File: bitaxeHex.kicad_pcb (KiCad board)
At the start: 4 copper layers, 84.5 x 129.5 mm, 384 parts, among them J1 Screw Terminal, J2 Conn_01x01, J3 TC2030-IDC, J4 USB_C_Receptacle_USB2.0, J5 Conn_01x04, J6 Conn_01x04, J7 Conn_01x04, J8 ST7789 176x320, Q1 NTMFS5C673NLT1G, Q2 CSD17577Q5A, Q3 NTMFS5C673NLT1G, Q4 CSD17577Q5A, Q5 BSS123, Q6 2N7002K, SW1 EVQ-9P701P, SW2 EVQ-9P701P, U1 uA7805, U10 TMP1075, U11 TMP1075, U12 EMC2302, U13 BM1366_mode1, U14 ADP171AUJ-R7, U15 ADP171AUJ-R7, U16 BM1366_mode1, U17 25MHz, U18 TLV3544, U19 BM1366_mode0, U2 RT9080-33GJ5, U20 ADP171AUJ-R7, U21 ADP171AUJ-R7, U22 BM1366_mode0, U23 TLV3544, U24 BM1366_mode1, U25 ADP171AUJ-R7, U26 ADP171AUJ-R7, U27 BM1366_mode1, U28 25MHz, U3 INA219AIDCNR, U4 TPS40305, U5 MIC5504, U6 DS4432U+, U7 SN74AVC4T774, U8 25MHz, U9 ESP32-S3-WROOM-1, Y1 32.768kHz

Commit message: Fix some part numbers in the BOM
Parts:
- U3: value INA219AIDCNR -> INA219AID
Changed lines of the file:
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@@
     (descr "SOIC, 8 Pin (JEDEC MS-012AA, https://www.analog.com/media/en/package-pcb-resources/package/pkg_pdf/soic_narrow-r/r_8.pdf), generated with kicad-footprint-generator ipc_gullwing_generator.py")
     (tags "SOIC SO")
-    (property "DK" "296-23770-1-ND")
-    (property "PARTNO" "INA219AIDCNR")
+    (property "DK" "296-33291-5-ND")
+    (property "PARTNO" "INA219AID")
     (property "Sheetfile" "power.kicad_sch")
     (property "Sheetname" "Power")
@@
         (effects (font (size 1 1) (thickness 0.15)))
     )
-    (fp_text value "INA219AIDCNR" (at 0 3.4 -90) (layer "F.Fab")
+    (fp_text value "INA219AID" (at 0 3.4 -90) (layer "F.Fab")
         (effects (font (size 1 1) (thickness 0.15)))
     )

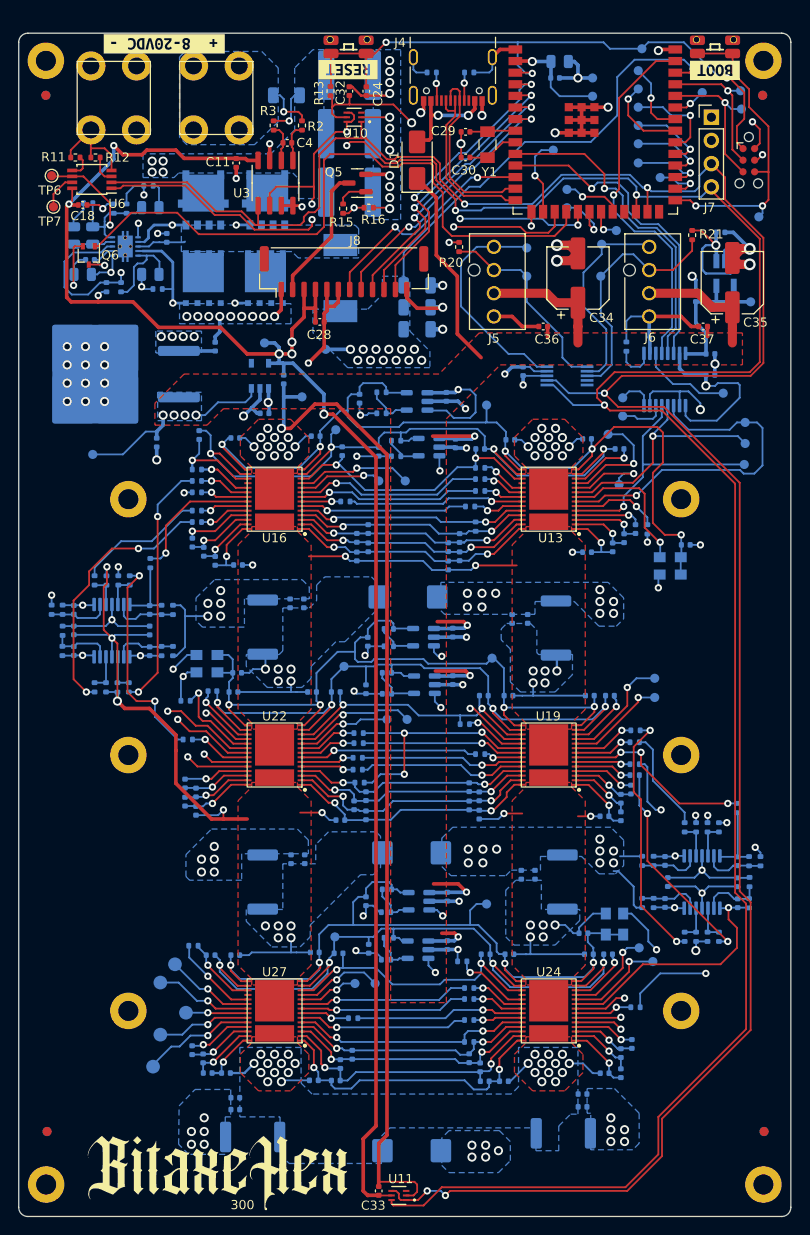
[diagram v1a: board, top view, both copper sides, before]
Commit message: mounting holes and fiducials
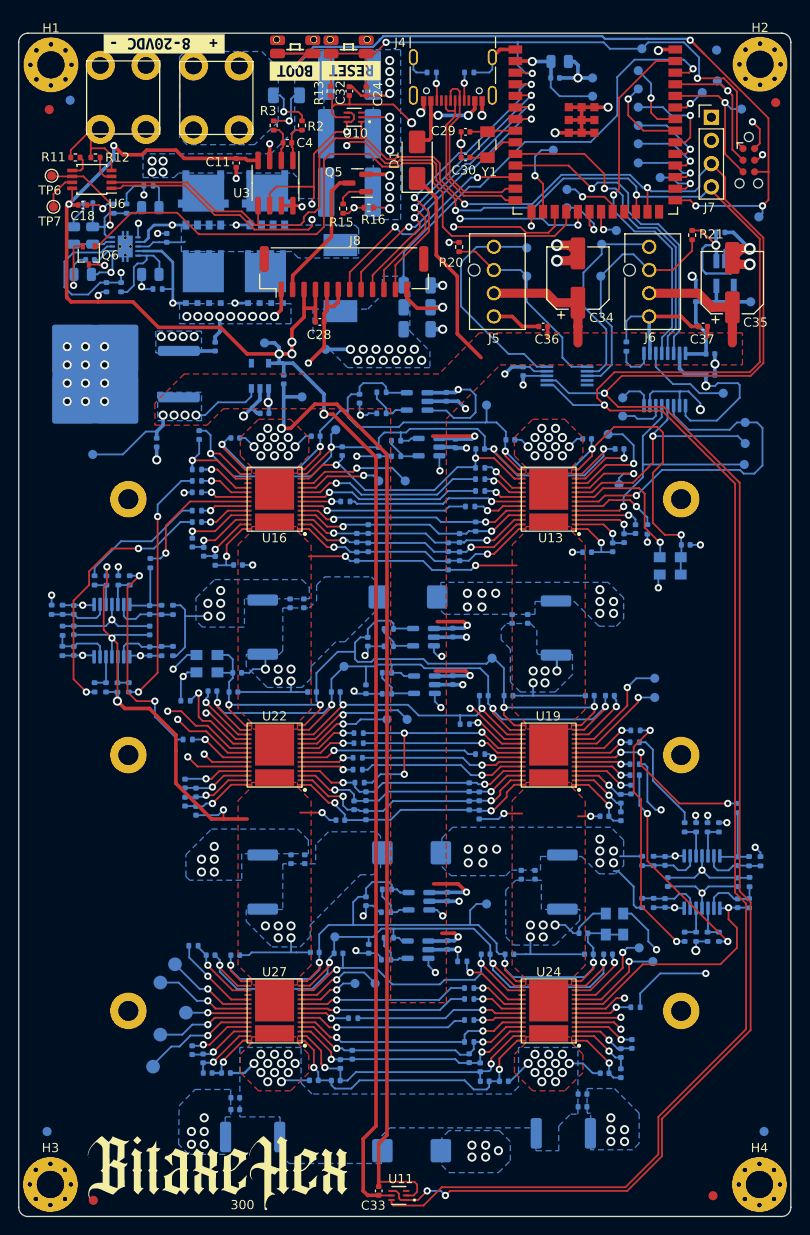
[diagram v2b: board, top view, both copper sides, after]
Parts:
- H1, H2, H3, H4: footprint bitaxe:4mm_mounting -> MountingHole:MountingHole_3mm_Pad_Via
- R25, R55, R87: value 130k 1% -> 69.8k 1%
- moved kibuzzard-65356D5C 46.0 mm to (80.2, 50.1)
- moved SW2 46.0 mm to (80.2, 47.5)
- moved FID7 9.08 mm to (58.2, 173.7)
- moved FID5 8.98 mm to (126.0, 173.2)
- moved FID8 7.06 mm to (126.4, 47.9)
- moved TP14 2.77 mm to (126.5, 51.2)
- moved FID6 2.71 mm to (55.6, 53.3)
- moved FID1 1.64 mm to (132.8, 53.6)
- moved FID3 1.60 mm to (53.3, 54.4)
- moved J2 1.03 mm to (61.4, 53.0)
- moved H1 0.70 mm to (53.5, 49.5)
- moved H2 0.57 mm to (131.1, 49.4)
- moved H3 0.47 mm to (53.5, 172.0)
- moved H4 0.44 mm to (131.1, 172.0)
- moved kibuzzard-65356D4E 0.34 mm to (86.4, 50.1)
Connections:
- net /BM1366-1/1V2 renamed /BM1366-1/1V8
- net /BM1366-2/1V2 renamed /BM1366-2/1V8
- net /BM1366-3/1V2 renamed /BM1366-3/1V8
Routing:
- net /ESP32/IO0: track 35.1 -> 85.8 mm, vias 2 -> 4
- net GND: track 427.1 -> 427.7 mm
- net /ESP32/EN: track 69.0 -> 69.5 mm

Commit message: fix mounting holes size/spacing, add pullup to PWR_EN signal
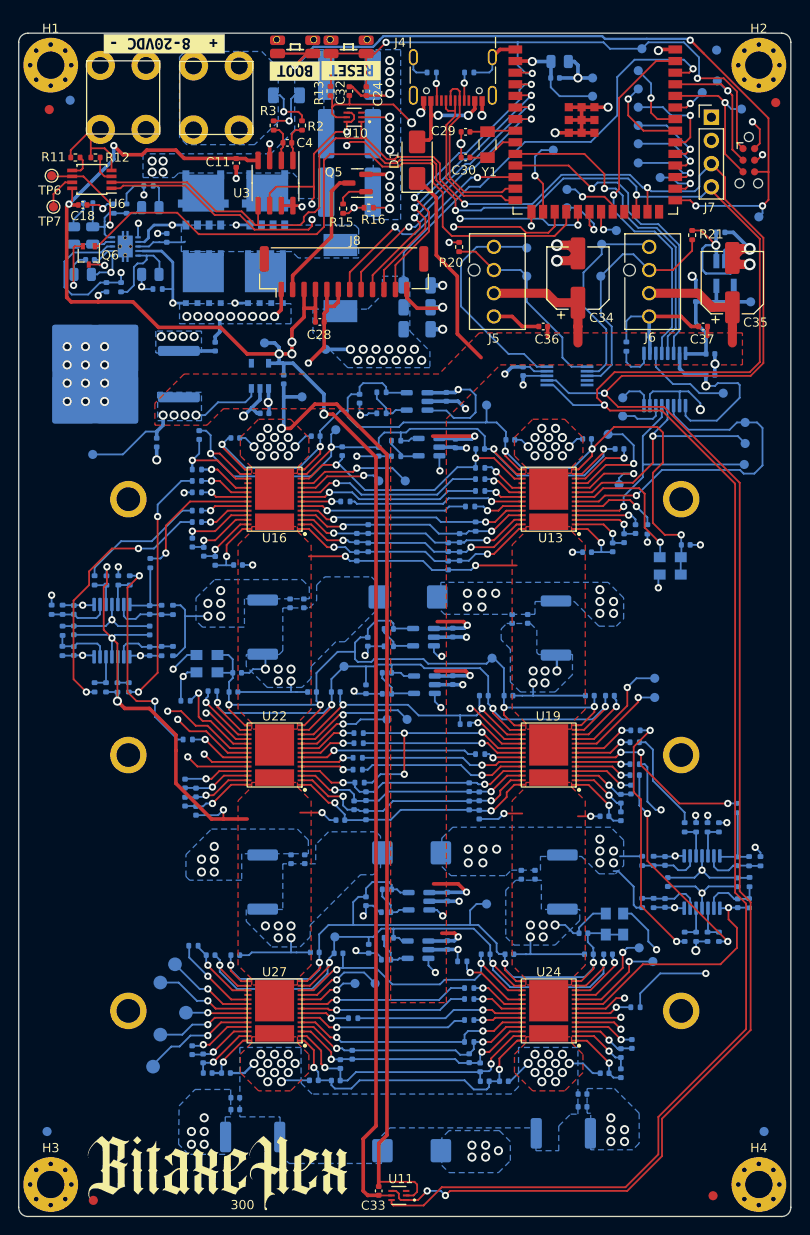
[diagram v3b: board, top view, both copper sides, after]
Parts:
- moved H2 0.16 mm to (131.0, 49.5)
- moved H4 0.06 mm to (131.0, 172.0)
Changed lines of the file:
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@@
   )
   (footprint "MountingHole:MountingHole_3mm_Pad_Via" (layer "F.Cu")
-    (at 53.52701 49.46301)
+    (at 53.5 49.5)
     (descr "Mounting Hole 3mm")
     (tags "mounting hole 3mm")
@@
   )
   (footprint "MountingHole:MountingHole_3mm_Pad_Via" (layer "F.Cu")
-    (at 131.064 172)
+    (at 131 172)
     (descr "Mounting Hole 3mm")
     (tags "mounting hole 3mm")
@@
         (effects (font (size 1 1) (thickness 0.15)))
     )
-    (pad "" thru_hole circle (at 0 0 180) (size 4 4) (drill 2.2) (layers "*.Cu" "*.Mask")
+    (pad "" thru_hole circle (at 0 0 180) (size 4 4) (drill 2.6) (layers "*.Cu" "*.Mask")
       (zone_connect 0))
   )
@@
         (effects (font (size 1 1) (thickness 0.15)))
     )
-    (pad "" thru_hole circle (at 0 0 180) (size 4 4) (drill 2.2) (layers "*.Cu" "*.Mask")
+    (pad "" thru_hole circle (at 0 0 180) (size 4 4) (drill 2.6) (layers "*.Cu" "*.Mask")
       (zone_connect 0))
   )
@@
         (effects (font (size 1 1) (thickness 0.15)))
     )
-    (pad "" thru_hole circle (at 0 0 180) (size 4 4) (drill 2.2) (layers "*.Cu" "*.Mask")
+    (pad "" thru_hole circle (at 0 0 180) (size 4 4) (drill 2.6) (layers "*.Cu" "*.Mask")
       (zone_connect 0))
   )
@@
         (effects (font (size 1 1) (thickness 0.15)))
     )
-    (pad "" thru_hole circle (at 0 0 180) (size 4 4) (drill 2.2) (layers "*.Cu" "*.Mask")
+    (pad "" thru_hole circle (at 0 0 180) (size 4 4) (drill 2.6) (layers "*.Cu" "*.Mask")
       (zone_connect 0))
   )
@@
         (effects (font (size 1 1) (thickness 0.15)))
     )
-    (pad "" thru_hole circle (at 0 0 180) (size 4 4) (drill 2.2) (layers "*.Cu" "*.Mask")
+    (pad "" thru_hole circle (at 0 0 180) (size 4 4) (drill 2.6) (layers "*.Cu" "*.Mask")
       (zone_connect 0))
   )
@@
   )
   (footprint "MountingHole:MountingHole_3mm_Pad_Via" (layer "F.Cu")
-    (at 131.13099 49.403)
+    (at 131 49.5)
     (descr "Mounting Hole 3mm")
     (tags "mounting hole 3mm")
@@
   )
   (footprint "MountingHole:MountingHole_3mm_Pad_Via" (layer "F.Cu")
-    (at 53.467 171.994)
+    (at 53.5 172)
     (descr "Mounting Hole 3mm")
     (tags "mounting hole 3mm")
@@
         (effects (font (size 1 1) (thickness 0.15)))
     )
-    (pad "" thru_hole circle (at 0 0 180) (size 4 4) (drill 2.2) (layers "*.Cu" "*.Mask")
+    (pad "" thru_hole circle (at 0 0 180) (size 4 4) (drill 2.6) (layers "*.Cu" "*.Mask")
       (zone_connect 0))
   )
@@
   )
   (dimension (type orthogonal) (layer "User.2")
-    (pts (xy 131.064 172) (xy 131.13099 49.403))
-    (height 18.1)
-    (orientation 1)
-    (gr_text "122.5970 mm" (at 148.014 110.7015 90) (layer "User.2")
-      (effects (font (size 1 1) (thickness 0.15)))
-    )
-    (format (prefix "") (suffix "") (units 3) (units_format 1) (precision 4))
-    (style (thickness 0.15) (arrow_length 1.27) (text_position_mode 0) (extension_height 0.58642) (extension_offset 0.5) keep_text_aligned)
-  )
-  (dimension (type orthogonal) (layer "User.2")
     (pts (xy 122.5 153) (xy 122.5 170))
     (height 20.8)
@@
   )
   (dimension (type orthogonal) (layer "User.2")
-    (pts (xy 53.467 171.994) (xy 131.064 172))
-    (height 16)
+    (pts (xy 53.5 171.994) (xy 131 172))
+    (height 15.906)
     (orientation 0)
-    (gr_text "77.5970 mm" (at 92.2655 186.844) (layer "User.2")
+    (gr_text "77.5000 mm" (at 92.25 186.75) (layer "User.2")
       (effects (font (size 1 1) (thickness 0.15)))
     )
@@
       (effects (font (size 1 1) (thickness 0.15)))
     )
+    (format (prefix "") (suffix "") (units 3) (units_format 1) (precision 4))
+    (style (thickness 0.15) (arrow_length 1.27) (text_position_mode 0) (extension_height 0.58642) (extension_offset 0.5) keep_text_aligned)
+  )
+  (dimension (type orthogonal) (layer "User.2")
+    (pts (xy 131 49.5) (xy 131 172))
+    (height 19.4)
+    (orientation 1)
+    (gr_text "122.5000 mm" (at 149.25 110.75 90) (layer "User.2")
+      (effects (font (size 1 1) (thickness 0.15)))
+    )

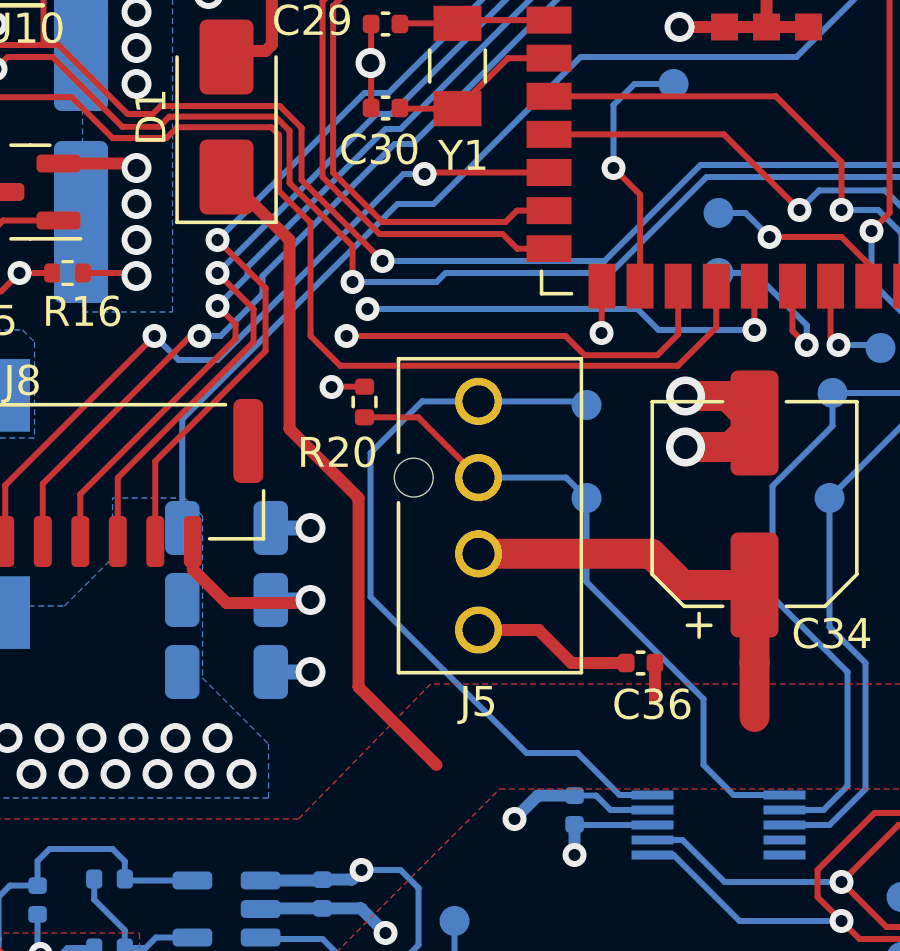
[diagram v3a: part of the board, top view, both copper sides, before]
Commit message: add PWR_EN pullup resistor to PCB layout
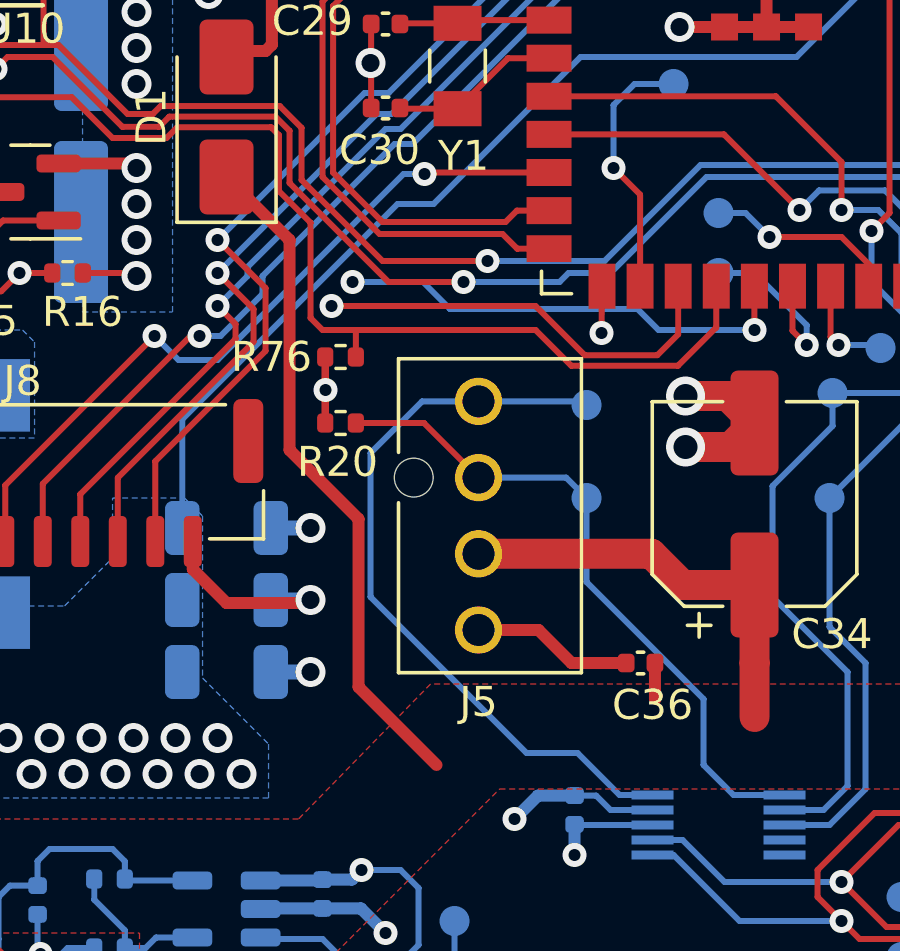
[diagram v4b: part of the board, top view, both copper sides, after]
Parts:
- added R76: 10K, Resistor_SMD:R_0402_1005Metric, F.Cu at (97.4, 67.9)
- moved R20 1.06 mm to (97.4, 70.1), turned to 180 degrees
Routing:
- net /3V3: track 257.0 -> 258.4 mm
- net /ESP32/TFT_BLK: track 28.3 -> 29.1 mm
- net /SDA: track 275.8 -> 275.1 mm
- net /ESP32/PWR_EN: track 71.2 -> 71.8 mm

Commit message: Start working on changelist for v301
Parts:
- moved TP1 14.9 mm to (72.5, 88.3), turned to 0 degrees
- moved C12 4.71 mm to (69.7, 89.8), turned to 0 degrees
- moved TP7 3.71 mm to (52.9, 61.4)
- moved TP6 3.47 mm to (52.9, 58.2)
- moved C65 1.54 mm to (69.5, 91.5), turned to 180 degrees
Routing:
- net /VDD: track 162.2 -> 110.0 mm, vias 41 -> 42
- net /5V: track 133.3 -> 126.9 mm
- net /Power/OUT0: track 21.8 -> 24.7 mm
- net /BM1366-1/0V8: track 80.5 -> 78.3 mm
- net GND: track 427.7 -> 426.2 mm
- net /Power/OUT1: track 3.98 -> 3.33 mm
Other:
- board text added: "301"
- board text removed: "300"
